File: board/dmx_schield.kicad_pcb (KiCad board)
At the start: 2 copper layers, 101.6 x 78.7 mm, 96 parts, among them J1 Conn_01x17, J2 Conn_01x17, J250 Conn_01x01, J251 Conn_01x01, J30 Conn_01x04, J40 Conn_01x06, J50 Conn_01x02, J60 Conn_01x03, Q1 BSR14, Q50 IRLML5203, SW1 SW_Push, SW2 SW_Push, SW3 SW_Push, SW4 SW_Push, U1 TEC 2-2411WI, U11 DCDC-SIP7-1-2-4-6, U140 LM317_3PinPackage, U3 LTV-847S, U5 LTV-827S, U6 ADUM1301, U60 MAX481E, U61 74LVC2G34, U7 REE-0505S/1S7E_0505S1.5UP

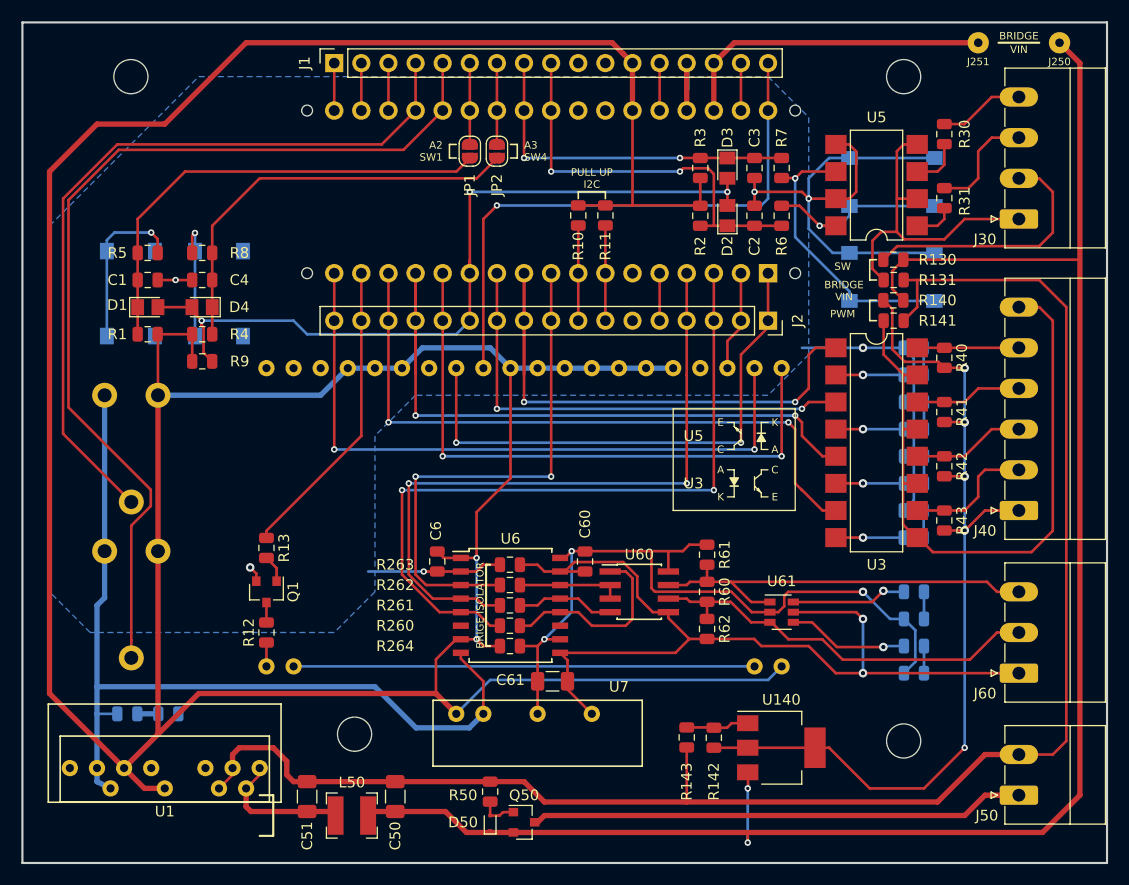
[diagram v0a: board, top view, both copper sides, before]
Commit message: fixed footprint SIL7, minor improvements, updated doc
fixed wrong pinout of SIL7 footprints and improved genral bnoard
layout and silk layer. Completed description of hardware. Added
a ods with the article numbers of the parts ordered @ reichelt.de.

This PCB verision will be manufactured and unploaded to aisler.net.
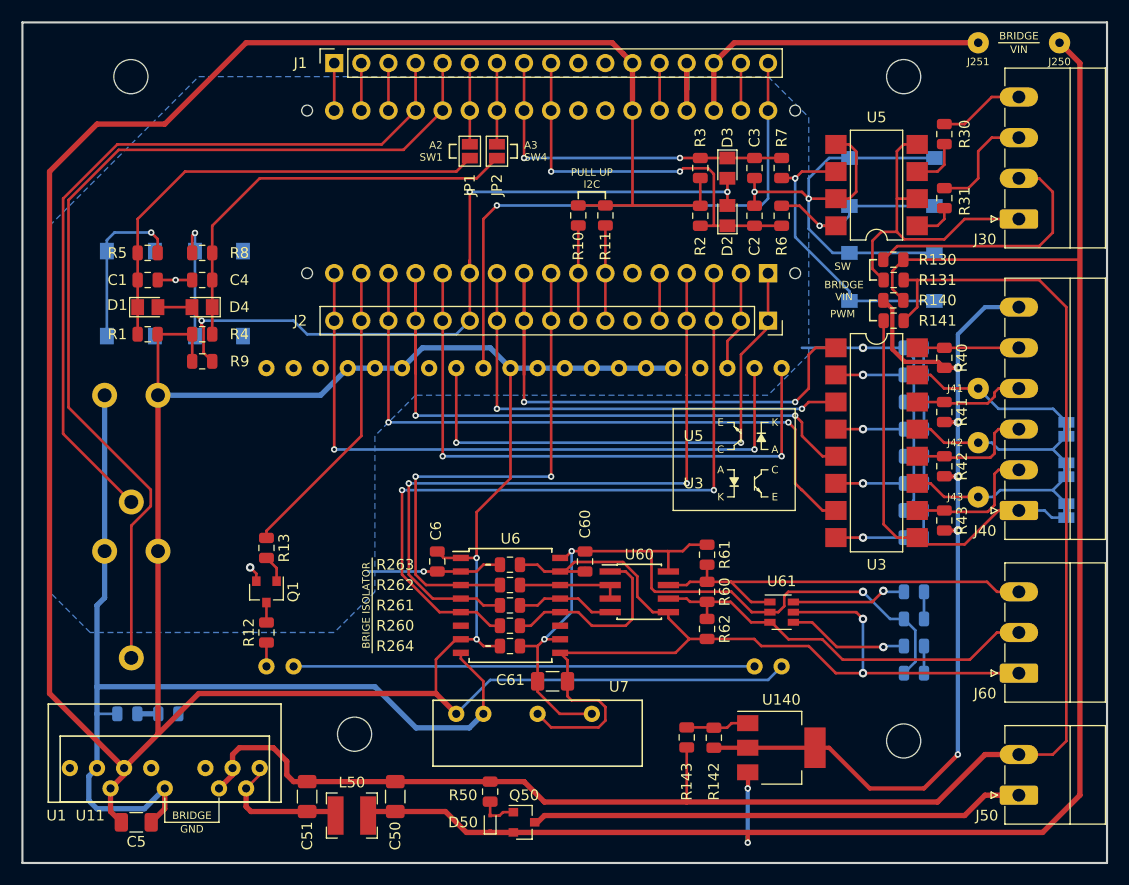
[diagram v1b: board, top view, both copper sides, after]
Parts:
- added C5: 10uF, Capacitor_SMD:C_1206_3216Metric, F.Cu at (48.8, 163.8)
- added J41: Conn_01x01, Connector_Wire:SolderWirePad_1x01_Drill0.8mm, F.Cu at (127.6, 123.2)
- added J42: Conn_01x01, Connector_Wire:SolderWirePad_1x01_Drill0.8mm, F.Cu at (127.6, 128.3)
- added J43: Conn_01x01, Connector_Wire:SolderWirePad_1x01_Drill0.8mm, F.Cu at (127.6, 133.3)
- added JP40: SolderJumper_2_Bridged, Jumper:SolderJumper-2_P1.3mm_Bridged_Pad1.0x1.5mm, B.Cu at (135.9, 127.0)
- added JP41: SolderJumper_2_Bridged, Jumper:SolderJumper-2_P1.3mm_Bridged_Pad1.0x1.5mm, B.Cu at (135.9, 130.8)
- added JP42: SolderJumper_2_Bridged, Jumper:SolderJumper-2_P1.3mm_Bridged_Pad1.0x1.5mm, B.Cu at (135.9, 134.6)
- JP1, JP2: footprint Jumper:SolderJumper-2_P1.3mm_Open_RoundedPad1.0x1.5mm -> Jumper:SolderJumper-2_P1.3mm_Open_Pad1.0x1.5mm
- LCD1: footprint my_lib:EA DOGM 162 -> my_lib:EA_DOGM_162
- R30, R31: value 540@12V -> 560@12V
- R61, R62: value 562 -> 560
- U1: value TEC 2-2411WI -> DCDC-SIP8-1-2-(3)-6-7
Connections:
- net /3_GND renamed /30_GND
- net /3_VCC renamed /30_VCC
- net /I_SW_DOWN renamed /I_SW3_DOWN
- net /I_SW_UP renamed /I_SW2_UP
- C60 pad 1: Net-(C60-Pad1) -> /60_VCC
- C60 pad 2: /6_GND -> /60_GND
- C61 pad 1: /6_GND -> /60_GND
- C61 pad 2: Net-(C60-Pad1) -> /60_VCC
- J40 pad 1: /4_VDD -> /40_GND
- J40 pad 6: /4_GND -> /40_VDD
- J60 pad 1: /6_GND -> /60_GND
- R140 pad 1: /4_VDD -> /40_VDD
- R141 pad 1: /4_GND -> /40_GND
- R142 pad 1: /4_VDD -> /40_VDD
- R263 pad 1: /6_GND -> /60_GND
- R264 pad 1: Net-(C60-Pad1) -> /60_VCC
- R40 pad 2: /4_VDD -> /40_VDD
- R41 pad 2: /4_VDD -> /40_VDD
- R42 pad 2: /4_VDD -> /40_VDD
- R43 pad 2: /4_VDD -> /40_VDD
- R61 pad 1: Net-(C60-Pad1) -> /60_VCC
- R62 pad 2: /6_GND -> /60_GND
- R63 pad 1: Net-(C60-Pad1) -> /60_VCC
- R64 pad 1: Net-(C60-Pad1) -> /60_VCC
- U11 pad 4: VCC -> GND
- U11 pad 6: GND -> VCC
- U140 pad 2: /4_VDD -> /40_VDD
- U3 pad 11: /4_GND -> Net-(J43-Pad1)
- U3 pad 13: /4_GND -> Net-(J42-Pad1)
- U3 pad 15: /4_GND -> Net-(J41-Pad1)
- U3 pad 9: /4_GND -> /40_GND
- U6 pad 10: Net-(C60-Pad1) -> /60_VCC
- U6 pad 15: /6_GND -> /60_GND
- U6 pad 16: Net-(C60-Pad1) -> /60_VCC
- U6 pad 9: /6_GND -> /60_GND
- U60 pad 5: /6_GND -> /60_GND
- U60 pad 8: Net-(C60-Pad1) -> /60_VCC
- U61 pad 2: Net-(C60-Pad1) -> /60_VCC
- U61 pad 5: /6_GND -> /60_GND
- U7 pad 4: Net-(C60-Pad1) -> /60_GND
- U7 pad 6: /6_GND -> /60_VCC
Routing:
- net /60_GND: track 0.00 -> 97.6 mm, vias 0 -> 2
- net /40_VDD: track 0.00 -> 87.5 mm, vias 0 -> 5
- net /6_GND: track 87.0 -> 0.00 mm, vias 2 -> 0
- net /4_VDD: track 86.2 -> 0.00 mm, vias 5 -> 0
- net /60_VCC: track 0.00 -> 76.2 mm, vias 0 -> 3
- net Net-(C60-Pad1): track 72.3 -> 0.00 mm, vias 3 -> 0
- net /4_GND: track 63.2 -> 0.00 mm
- net /40_GND: track 0.00 -> 38.9 mm
- net Net-(J42-Pad1): track 0.00 -> 18.0 mm
- net Net-(J43-Pad1): track 0.00 -> 17.1 mm
- net Net-(J41-Pad1): track 0.00 -> 15.8 mm
- net GND: track 185.1 -> 197.7 mm
- net /I_PWM4: track 12.2 -> 13.8 mm
- net VCC: track 360.9 -> 362.3 mm
- net /I_PWM3: track 10.6 -> 11.8 mm
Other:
- board text added: "BUTTONS 4 SW3 3 SW2 2 VDD 1 GND"
- board text added: "DMX 3 DMX- 2 DMX+ 1 GND"
- board text added: "GND"
- board text added: "PWM/IO 6 VCC 5 PWM1 4 PWM2 3 PWM3 2 PWM4 1 GND"
- board text added: "V2.0-03/05/2020"
- board text removed: "BUTTONS 1 GND 2 VDD 3 SW2 4 SW3"
- board text removed: "DMX 1 GND 2 DMX+ 3 DMX-"
- board text removed: "PWM/IO 1 VDD 2 PWM4 3 PWM3 4 PWM2 5 PWM1 6 GND"
- board text removed: "V2.0.0alpha-01/05/2020"
